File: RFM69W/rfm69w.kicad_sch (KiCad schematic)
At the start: 9 parts, among them J1 Conn1, J2 Conn2, J3 U.FL / IPEX, J4 SMA, U1 RFM69W

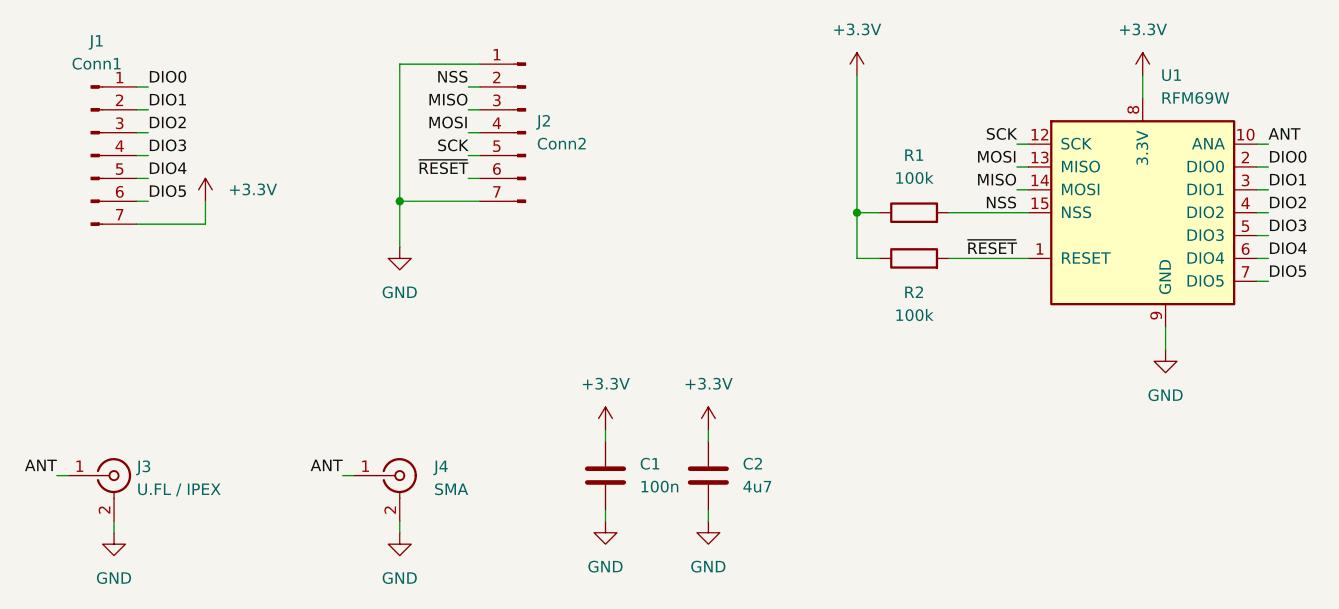
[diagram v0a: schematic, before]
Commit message: Updated the RFM69W and RFM95W/RFM96W board layouts.
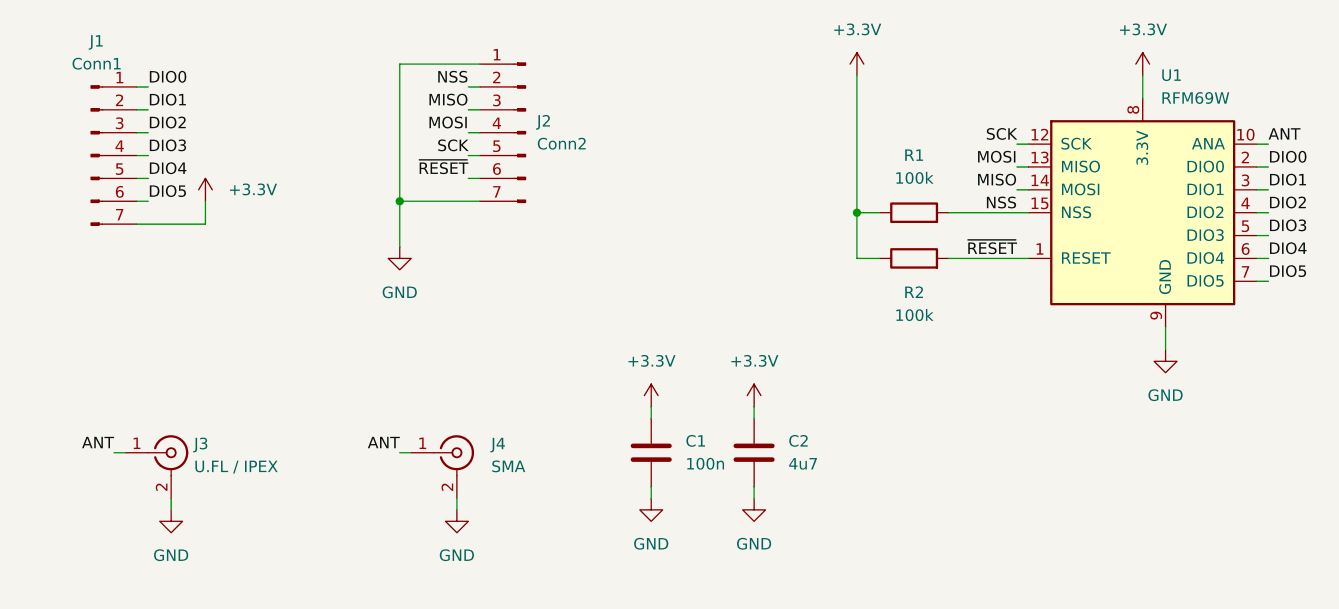
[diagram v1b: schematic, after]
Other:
- moved on the sheet: C1, C2, J3, J4
